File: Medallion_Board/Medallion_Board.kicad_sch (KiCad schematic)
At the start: 125 parts, among them IC1 Wio-SX1262, J1 SWD HEADER, J2 EXPANSION, J3 IPEX, J4 FH12-24S-0.5SH_55_, P1 JST_BTN_1, P2 JST_BTN_2, P3 JST_BTN_3, Q1 DMG3415U, Q2 Si1308EDL, U1 MDBT50Q-1MV2, U2 MAX17048G_T10, U3 LC86LICMD, U4 RT9080-33GJ5, U5 MCP73831T-2ACI_OT, U6 BNO085, U7 DRV2605LDGSR, U8 MX25R6435FZAIH0, X1 USB4085-GF-A, Y1 32.768KHZ

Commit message: Move to hierarchical schematic
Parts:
- removed BATT1: JST_PH, S2B-PH-SM4-TB_LF__SN_:JST_S2B-PH-SM4-TB_LF__SN_, symbol S2B-PH-SM4-TB_LF__SN_:S2B-PH-SM4-TB_LF__SN_
- removed C10, C15, C16, C17, C18, C19, C20, C21, C22, C23, C31, C32, C33, C34, C35, C36, C37, C38, C41: 0.1uF, Capacitor_SMD:C_0402_1005Metric, symbol Adafruit ESP32-S3 8MB No PSRAM-eagle-import:CAP_CERAMIC0805-NOOUTLINE
- removed C11, C12, C13, C14, C5, C9: 10uF, Capacitor_SMD:C_0805_2012Metric, symbol Adafruit ESP32-S3 8MB No PSRAM-eagle-import:CAP_CERAMIC0805-NOOUTLINE
- removed C24, C25, C27, C28, C7: 0.1uF, Capacitor_SMD:C_0402_1005Metric, symbol Adafruit ESP32-S3 8MB No PSRAM-eagle-import:CAP_CERAMIC0603_NO
- removed C26: 22uF, Capacitor_SMD:C_0402_1005Metric, symbol Adafruit ESP32-S3 8MB No PSRAM-eagle-import:CAP_CERAMIC0805-NOOUTLINE
- removed C29, C30: NM, Capacitor_SMD:C_0402_1005Metric, symbol Adafruit ESP32-S3 8MB No PSRAM-eagle-import:CAP_CERAMIC0805-NOOUTLINE
- removed C39, C40, C42, C45, C46, C47, C48, C49, C50, C51, C6: 1uF, Capacitor_SMD:C_0603_1608Metric, symbol Adafruit ESP32-S3 8MB No PSRAM-eagle-import:CAP_CERAMIC0603_NO
- removed C43, C44: 4.7uF, Capacitor_SMD:C_0603_1608Metric, symbol Adafruit ESP32-S3 8MB No PSRAM-eagle-import:CAP_CERAMIC0603_NO
- removed C8: 100mF, KW-5R5C104-R:CAPPRD500W60D1000H3150, symbol XH414HG-IV01E:XH414HG-IV01E
- removed CHG1: ORANGE, LED_SMD:LED_0603_1608Metric, symbol Adafruit ESP32-S3 8MB No PSRAM-eagle-import:LED0603_NOOUTLINE
- removed D1: MBR0540, Diode_SMD:D_SOD-123, symbol Adafruit ESP32-S3 8MB No PSRAM-eagle-import:DIODE-SCHOTTKYSOD-123
- removed D10, D11, D13, D14, D15, D16, D17, D18, D19, D20, D3, D4, D5, D6, D7, D8, D9: WS2812B2020, WS2812B2020:LED_WS2812B2020, symbol WS2812B2020:WS2812B2020
- removed D12: TPD1E05U06DPYR, TPD1E05U06DPYR:DIO_TPD1E05U06DPYR, symbol TPD1E05U06DPYR:TPD1E05U06DPYR
- removed D2: BAV199, BAV199:SOT23, symbol BAV199:BAV199
- removed D21, D22, D23: MBR0530, Diode_SMD:D_SOD-123, symbol Diode:MBR0530
- removed IC1: Wio-SX1262, 114993390:114993390, symbol 114993390:114993390
- removed J3: IPEX, RECE.20369:RECE20369001E01, symbol RECE_20369_001E_01:RECE.20369.001E.01
- removed J4: FH12-24S-0.5SH_55_, FH12-24S-0.5SH_55_:HRS_FH12-24S-0.5SH_55_, symbol FH12-24S-0.5SH_55_:FH12-24S-0.5SH_55_
- removed L1: 10uH, LQM18DN100M70L:INDC1608X95N, symbol LQM18DN100M70L:LQM18DN100M70L
- removed L2: 47uH 500mA, symbol LQM18DN100M70L:LQM18DN100M70L
- removed LRA1: Conn_01x02, Connector_PinHeader_2.54mm:PinHeader_1x02_P2.54mm_Vertical, symbol Connector_Generic:Conn_01x02
- removed ONOFF1: JST_ONOFF, SM02B-GHS-TB:JST_SM02B-GHS-TB, symbol SM02B-GHS-TB:SM02B-GHS-TB
- removed P1: JST_BTN_1, SM02B-GHS-TB:JST_SM02B-GHS-TB, symbol SM02B-GHS-TB:SM02B-GHS-TB
- removed P2: JST_BTN_2, SM02B-GHS-TB:JST_SM02B-GHS-TB, symbol SM02B-GHS-TB:SM02B-GHS-TB
- removed P3: JST_BTN_3, SM02B-GHS-TB:JST_SM02B-GHS-TB, symbol SM02B-GHS-TB:SM02B-GHS-TB
- removed Q1: DMG3415U, DMG3415U-7:SOT95P240X105-3N, symbol Adafruit ESP32-S3 8MB No PSRAM-eagle-import:MOSFET-P
- removed Q2: Si1308EDL, Package_TO_SOT_SMD:SOT-323_SC-70, symbol Transistor_FET:Si1308EDL
- removed R10, R11: 1K, Resistor_SMD:R_0603_1608Metric, symbol Adafruit ESP32-S3 8MB No PSRAM-eagle-import:RESISTOR_0603_NOOUT
- removed R12, R13, R16, R20, R22: 10K, Resistor_SMD:R_0603_1608Metric, symbol Adafruit ESP32-S3 8MB No PSRAM-eagle-import:RESISTOR_0603_NOOUT
- removed R14: 0R, Resistor_SMD:R_0402_1005Metric, symbol Adafruit ESP32-S3 8MB No PSRAM-eagle-import:RESISTOR_0603_NOOUT
- removed R15: 500R, Resistor_SMD:R_0603_1608Metric, symbol Adafruit ESP32-S3 8MB No PSRAM-eagle-import:RESISTOR_0603_NOOUT
- removed R17, R18: 5K, Resistor_SMD:R_0603_1608Metric, symbol Adafruit ESP32-S3 8MB No PSRAM-eagle-import:RESISTOR_0603_NOOUT
- removed R19, R21: 27R, Resistor_SMD:R_0603_1608Metric, symbol Adafruit ESP32-S3 8MB No PSRAM-eagle-import:RESISTOR_0603_NOOUT
- removed R23: 1M, Resistor_SMD:R_0603_1608Metric, symbol Adafruit ESP32-S3 8MB No PSRAM-eagle-import:RESISTOR_0603_NOOUT
- removed R24: 2.2R, Resistor_SMD:R_0603_1608Metric, symbol Adafruit ESP32-S3 8MB No PSRAM-eagle-import:RESISTOR_0603_NOOUT
- removed R9: 100K, Resistor_SMD:R_0603_1608Metric, symbol Adafruit ESP32-S3 8MB No PSRAM-eagle-import:RESISTOR_0603_NOOUT
- removed U1: MDBT50Q-1MV2, MDBT50Q-1MV2:XCVR_MDBT50Q-1MV2, symbol MDBT50Q-1MV2:MDBT50Q-1MV2
- removed U2: MAX17048G_T10, MAX17048G_T10:SON50P200X200X80-9N, symbol MAX17048G_T10:MAX17048G_T10
- removed U3: LC86LICMD, LC86LICMD:MODULE_LC86LICMD, symbol LC86LICMD:LC86LICMD
- removed U4: RT9080-33GJ5, RT9080-33GJ5:SOT94P280X100-5N, symbol Adafruit ESP32-S3 8MB No PSRAM-eagle-import:VREG_SOT23-5
- removed U5: MCP73831T-2ACI_OT, MCP73831T-2ACI_OT:SOT95P280X145-5N, symbol MCP73831T-2ACI_OT:MCP73831T-2ACI_OT
- removed U6: BNO085, BNO085:IC_BNO085, symbol BNO085:BNO085
- removed U7: DRV2605LDGSR, DRV2605LDGSR:SOP50P490X110-10N, symbol DRV2605LDGSR:DRV2605LDGSR
- removed U8: MX25R6435FZAIH0, MX25R6435FZAIH0:SON80P400X400X60-9N, symbol MX25R6435FZAIH0:MX25R6435FZAIH0
- added C5: 1uF, Capacitor_SMD:C_0603_1608Metric, symbol Adafruit ESP32-S3 8MB No PSRAM-eagle-import:CAP_CERAMIC0603_NO
- added C6: 0.1uF, Capacitor_SMD:C_0402_1005Metric, symbol Adafruit ESP32-S3 8MB No PSRAM-eagle-import:CAP_CERAMIC0805-NOOUTLINE
- added U1: BMD-340-A-R, BMD_340_A_R:RIGADO_BMD-340-A-R, symbol BMD-340-A-R:BMD-340-A-R
- added U2: MX25R6435FZAIH0, MX25R6435FZAIH0:SON80P400X400X60-9N, symbol MX25R6435FZAIH0:MX25R6435FZAIH0
- C1, C2: value 12pF -> 10uF; footprint Capacitor_SMD:C_0402_1005Metric -> Capacitor_SMD:C_0805_2012Metric; MPN GMC04CG120J6R3NT -> CL21A106KPFNNNG
- C3, C4: value 10uF -> 12pF; footprint Capacitor_SMD:C_0805_2012Metric -> Capacitor_SMD:C_0402_1005Metric; MPN 0805W106K6R3CC -> C0402C0G120J500NTB; PRICE 0.07 -> 0.00371
- R2: value 10K -> 5K; MPN RC0603FR-0710KL -> RT0603BRE075KL
- R3: value 10K -> 27R; MPN RC0603FR-0710KL -> RC0603FR-0727RL
- R4: value 100K -> 27R; MPN RC0603FR-07100KL -> RC0603FR-0727RL
- R5: value 1K -> 5K; MPN RC0603FR-071KL -> RT0603BRE075KL
- R6, R7: value 5K -> 10K; MPN RT0603BRE075KL -> RC0603FR-0710KL
- R8: value 2K -> 10K; MPN RC0603FR-072KL -> RC0603FR-0710KL
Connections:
- net GPIO15 is gone; now on net GPIO17: J2.2 (Pin_2)
- net VHI is gone; now on net D-: R4.1
- net D+: now also R3.1, U1.68 (USB-D+)
- net D-: now also U1.67 (USB-D-)
- net FLASH_CS: now also R8.1, U2.1 (CS#)
- net FLASH_RST: now also U2.7 (RESET#/SIO3)
- net FLASH_WP: now also U2.3 (WP#/SIO2)
- net GND: now also C1.2, C2.2, C3.1, C4.1, R1.1, R2.1, C5.2, C6.2, U1.1 (GND), U1.16 (GND__5), U1.18 (GND__6), U1.2 (GND__1), U1.29 (GND__7), U1.3 (GND__2), U1.30 (GND__8), U1.4 (GND__3), U1.45 (GND__9), U1.46 (GND__10), U1.47 (GND__11), U1.5 (GND__4), U1.55 (GND__12), U2.4 (GND); no longer C1.1, C2.1, C3.2, C4.2, R7.2, R8.1
- net GPIO17: now also U1.35 (P0.17); no longer J2.4 (Pin_4)
- net GPS_ANT_ACTIVE: now also U1.11 (P0.30)
- net GPS_RESET: now also U1.12 (P0.31)
- net GPS_WAKEUP: now also U1.10 (P0.29)
- net NEOPIX: now also U1.34 (P0.16)
- net OSC1: now also C3.2, U1.13 (P0.00); no longer C1.2
- net OSC2: now also C4.2, U1.14 (P0.01); no longer C2.2
- net RXD_GPS: now also U1.23 (P0.07)
- net SCL: now also R6.2, U1.8 (P0.27); no longer R2.1
- net SDA: now also R7.2, U1.7 (P0.26); no longer R3.1
- net SPI_MISO: now also U1.40 (P0.22), U2.2 (SO/SIO1)
- net SPI_MOSI: now also U1.41 (P0.23), U2.5 (SI/SIO0)
- net SPI_SCK: now also U1.42 (P0.24), U2.6 (SCLK)
- net TXD_GPS: now also U1.22 (P0.06)
- net VBUS: now also C2.1, U1.66 (VBUS)
- net uC_RESET: now also R5.1, C5.1, U1.39 (P0.18); no longer R1.1
- net at J1.3 (Pin_3): now also U1.44 (SWDIO)
- net at J1.2 (Pin_2): now also U1.43 (SWCLK)
- net +3.3V: now reaches R8.2
- net +3.3V: now also C1.1, J1.1 (Pin_1), J2.7 (Pin_7), R5.2, R6.1, R7.1, C6.1, U1.17 (VCC1), U1.65 (VCCH1), U2.8 (VCC)
- net at R4.2: now also X1.B6 (DP2)
- net at X1.B5 (CC2): now also R2.2
- net at X1.A6 (DP1): now also R3.2
- net at X1.A5 (CC1): now also R1.2
- removed net 3.3V: C4.1, J1.1 (VCC), J2.7 (Pin_7), R1.2, R2.2, R3.2
- net GPIO14 renamed GPIO05
- net GPIO05: now also U1.21 (P0.05)
- net GPIO16 renamed GPIO19
- net GPIO19: now also U1.37 (P0.19)
- new net Communications/LORA_BUSY: U1.33 (P0.15)
- new net Communications/LORA_DIO1: U1.25 (P0.09)
- new net Communications/LORA_NRST: U1.26 (P0.10)
- new net Communications/LORA_NSS: U1.31 (P0.13)
- new net Communications/LORA_RF_SW: U1.32 (P0.14)
- new net Communications/SPI_MISO: U1.28 (P0.12)
- new net Communications/SPI_MOSI: U1.27 (P0.11)
- new net Communications/SPI_SCK: U1.24 (P0.08)
- new net GPIO20: J2.4 (Pin_4), U1.38 (P0.20)
- new net HAPTIC_EN: U1.15 (P0.02)
- new net Power and USB/LOW_BATT: U1.36 (P0.21)
- new net User IO/BNO_NINT: U1.48 (P1.05)
- new net User IO/BNO_NRST: U1.49 (P1.06)
- new net User IO/DISP_BS: U1.56 (P1.00)
- new net User IO/DISP_BUSY: U1.57 (P1.01)
- new net User IO/DISP_CS: U1.58 (P1.02)
- new net User IO/DISP_D/C: U1.59 (P1.03)
- new net User IO/DISP_RES: U1.60 (P1.04)
- new net User IO/USER_BTN_1: U1.50 (P1.07)
- new net User IO/USER_BTN_2: U1.51 (P1.08)
- new net User IO/USER_BTN_3: U1.52 (P1.09)
- no-connect marks 14 -> 15
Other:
- added sheet Communications (communications.kicad_sch)
- added sheet Power and USB (power.kicad_sch)
- added sheet User IO (user_io.kicad_sch)
- note added: "FUTURE EXPANSION BREAKOUT"
- note added: "LOW FREQUENCY PINS (<10kHz) P0.28-0.31, P0.02, P0.03, P0.09, P0.10 P1.01-1.07, P1.10-1.15"
- note added: "RESET"
- note removed: "1.0K = 1000mA"
- note removed: "10K = 100mA"
- note removed: "2.0K = 500mA"
- note removed: "5.0K = 200mA"
- note removed: "Adafruit estimate 20mA for typical use 20mA * 4 = 80mA LED load"
- note removed: "CHARGER"
- note removed: "E-INK DISPLAY"
- note removed: "FUEL GAUGE"
- note removed: "FUTURE-PROOFING BREAKOUT"
- note removed: "GNSS"
- note removed: "HAPTICS"
- note removed: "IMU SENSOR"
- note removed: "LIPO CHARGING AND REPORTING"
- note removed: "LORA RADIO"
- note removed: "NEEDS REVIEW https://files.waveshare.com/wiki/1.54inch%20e-Paper%20Module%20(G)/1.54inch_e-Paper_(G).pdf PAGE 44"
- note removed: "Neopixel Ring"
- note removed: "No more than 3 pixels will be driven at full brightness, or 8 at 1/2 brightness, at a time."
- note removed: "POWER AND FILTERING"
- note removed: "USER BUTTONS"
- note removed: "Unused but implemented just in case"
- note removed: "V_BCKP enables much faster location acquisition 30s -> 2s"
- note removed: "nRF52840 MODULE"
- moved on the sheet: J2

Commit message: Some minor cleaning
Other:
- note added: "The product here is a smart compass. It has GNSS and an IMU for positioning in the world, and LoRa and BLE for comms. It uses a ring of RGB LED, an e-ink display, and haptic feedback for user interaction, along with 3 buttons. Battery powered, with USB-C charging."
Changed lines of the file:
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@@
 		(title "Smart Compass")
 		(date "2026-06-04")
+		(rev "0.2")
 	)
 	(rectangle
@@
 		)
 	)
+	(text "The product here is a smart compass. \n\nIt has GNSS and an IMU for positioning in the world,\nand LoRa and BLE for comms. \n\nIt uses a ring of RGB LED, an e-ink display, and haptic \nfeedback for user interaction, along with 3 buttons. \n\nBattery powered, with USB-C charging."
+		(exclude_from_sim no)
+		(at 239.014 30.226 0)
+		(effects
+			(font
+				(size 1.27 1.27)
+			)
+		)
+	)
 	(text "LOW FREQUENCY PINS\n(<10kHz)\n\nP0.28-0.31, P0.02, P0.03, P0.09, P0.10\nP1.01-1.07, P1.10-1.15"
 		(exclude_from_sim no)
@@
 		(property "Value" "GND"
 			(at 138.43 34.29 0)
+			(hide yes)
 			(show_name no)
 			(do_not_autoplace no)
@@
 		(property "Value" "GND"
 			(at 172.72 154.94 0)
+			(hide yes)
 			(show_name no)
 			(do_not_autoplace no)
@@
 		(property "Value" "GND"
 			(at 274.32 76.2 0)
+			(hide yes)
 			(show_name no)
 			(do_not_autoplace no)
@@
 		(property "Value" "GND"
 			(at 275.59 160.02 0)
+			(hide yes)
 			(show_name no)
 			(do_not_autoplace no)
@@
 		(property "Value" "GND"
 			(at 270.51 76.2 0)
+			(hide yes)
 			(show_name no)
 			(do_not_autoplace no)
@@
 		(property "Value" "GND"
 			(at 207.01 110.49 0)
+			(hide yes)
 			(show_name no)
 			(do_not_autoplace no)
@@
 		(property "Value" "GND"
 			(at 36.83 58.42 0)
+			(hide yes)
 			(show_name no)
 			(do_not_autoplace no)
@@
 		(property "Value" "GND"
 			(at 132.08 33.02 0)
+			(hide yes)
 			(show_name no)
 			(do_not_autoplace no)
@@
 		(property "Value" "GND"
 			(at 118.11 152.4 0)
+			(hide yes)
 			(show_name no)
 			(do_not_autoplace no)
@@
 		(property "Value" "GND"
 			(at 72.39 43.18 0)
+			(hide yes)
 			(show_name no)
 			(do_not_autoplace no)
@@
 		(property "Value" "GND"
 			(at 250.19 105.41 0)
+			(hide yes)
 			(show_name no)
 			(do_not_autoplace no)

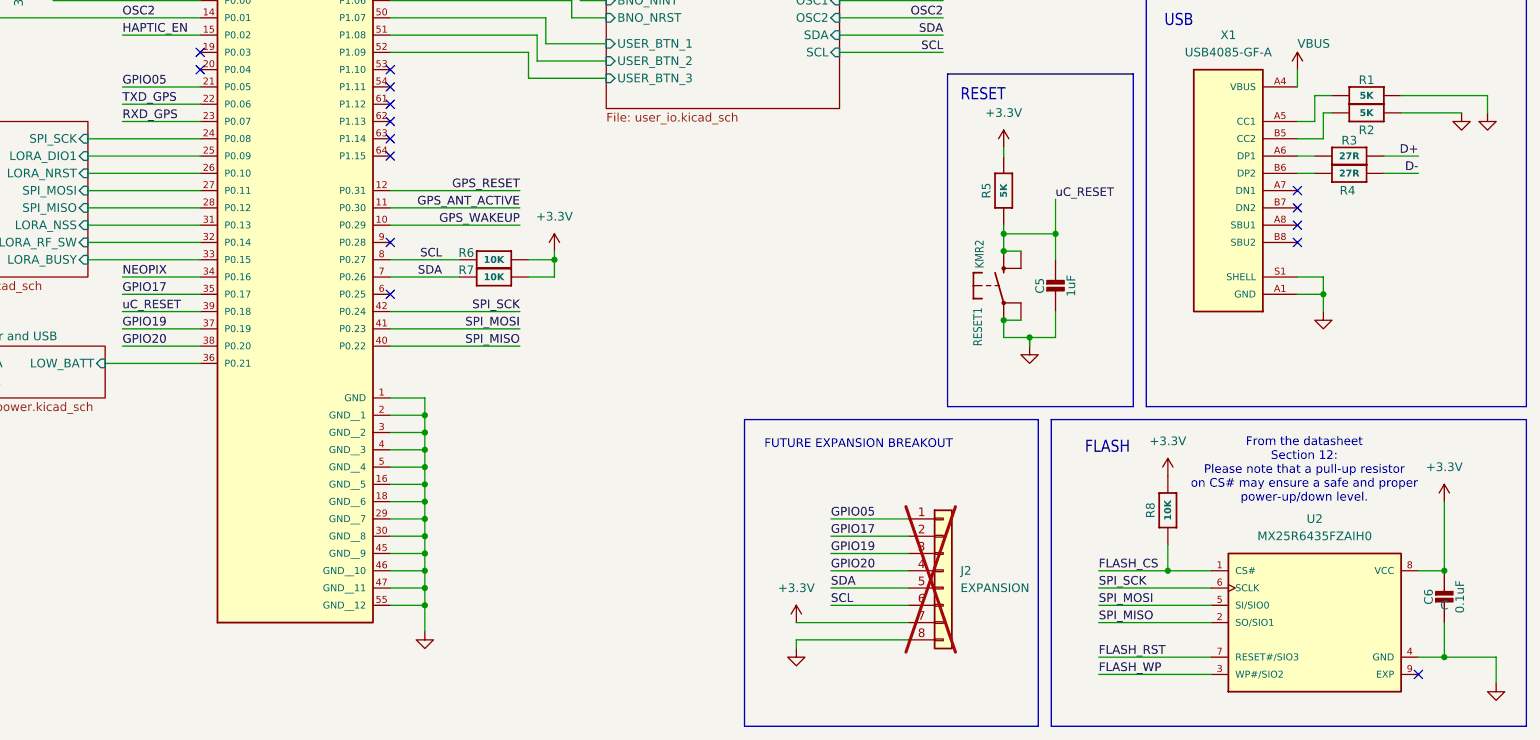
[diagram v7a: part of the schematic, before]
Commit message: Check over i2c, spi, and uart connections
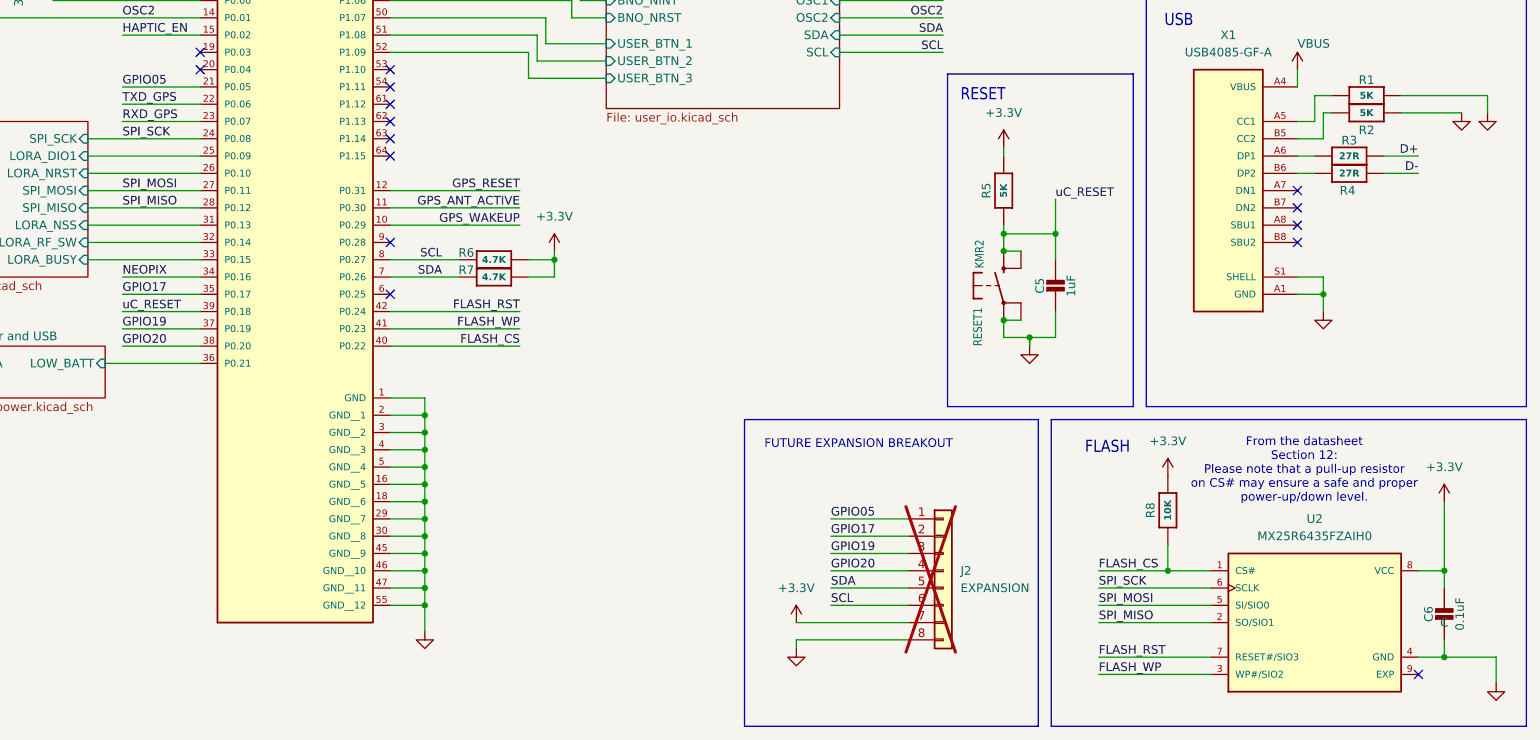
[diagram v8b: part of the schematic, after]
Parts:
- R6, R7: value 10K -> 4.7K; MPN RC0603FR-0710KL -> RC0603FR-074K7L
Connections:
- net Communications/SPI_MISO is gone; now on net SPI_MISO: U1.28 (P0.12)
- net Communications/SPI_MOSI is gone; now on net SPI_MOSI: U1.27 (P0.11)
- net Communications/SPI_SCK is gone; now on net SPI_SCK: U1.24 (P0.08)
- net FLASH_CS: now also U1.40 (P0.22)
- net FLASH_RST: now also U1.42 (P0.24)
- net FLASH_WP: now also U1.41 (P0.23)
- net SPI_MISO: no longer U1.40 (P0.22)
- net SPI_MOSI: no longer U1.41 (P0.23)
- net SPI_SCK: no longer U1.42 (P0.24)
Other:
- moved on the sheet: C6
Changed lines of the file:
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@@
 	)
 	(junction
-		(at 267.97 138.43)
-		(diameter 0)
-		(color 0 0 0 0)
-	)
-	(junction
 		(at 118.11 138.43)
 		(diameter 0)
@@
 	)
 	(junction
-		(at 267.97 151.13)
-		(diameter 0)
-		(color 0 0 0 0)
-	)
-	(junction
 		(at 118.11 135.89)
 		(diameter 0)
@@
 	)
 	(junction
+		(at 267.97 151.13)
+		(diameter 0)
+		(color 0 0 0 0)
+	)
+	(junction
 		(at 118.11 128.27)
 		(diameter 0)
@@
 	)
 	(junction
+		(at 267.97 138.43)
+		(diameter 0)
+		(color 0 0 0 0)
+	)
+	(junction
 		(at 207.01 104.14)
 		(diameter 0)
@@
 	(wire
 		(pts
-			(xy 267.97 146.05) (xy 267.97 151.13)
+			(xy 267.97 148.59) (xy 267.97 151.13)
 		)
 		(stroke
@@
 	(wire
 		(pts
+			(xy 113.03 100.33) (xy 132.08 100.33)
+		)
+		(stroke
+			(width 0)
+			(type default)
+		)
+	)
+	(wire
+		(pts
 			(xy 134.62 59.69) (xy 134.62 63.5)
 		)
@@
 	(wire
 		(pts
-			(xy 113.03 100.33) (xy 132.08 100.33)
-		)
-		(stroke
-			(width 0)
-			(type default)
-		)
-	)
-	(wire
-		(pts
 			(xy 250.19 97.79) (xy 246.38 97.79)
 		)
@@
 	(wire
 		(pts
+			(xy 113.03 102.87) (xy 132.08 102.87)
+		)
+		(stroke
+			(width 0)
+			(type default)
+		)
+	)
+	(wire
+		(pts
 			(xy 113.03 125.73) (xy 118.11 125.73)
 		)
@@
 	(wire
 		(pts
-			(xy 118.11 135.89) (xy 118.11 138.43)
+			(xy 113.03 105.41) (xy 132.08 105.41)
 		)
 		(stroke
@@
 	(wire
 		(pts
-			(xy 81.28 44.45) (xy 85.09 44.45)
+			(xy 118.11 135.89) (xy 118.11 138.43)
 		)
 		(stroke
@@
 	(wire
 		(pts
-			(xy 132.08 105.41) (xy 113.03 105.41)
+			(xy 81.28 44.45) (xy 85.09 44.45)
 		)
 		(stroke
@@
 	(wire
 		(pts
+			(xy 267.97 140.97) (xy 267.97 138.43)
+		)
+		(stroke
+			(width 0)
+			(type default)
+		)
+	)
+	(wire
+		(pts
 			(xy 43.18 44.45) (xy 41.91 44.45)
 		)
@@
 	(wire
 		(pts
-			(xy 113.03 102.87) (xy 132.08 102.87)
-		)
-		(stroke
-			(width 0)
-			(type default)
-		)
-	)
-	(wire
-		(pts
 			(xy 68.58 80.01) (xy 85.09 80.01)
 		)
@@
 		)
 	)
+	(label "FLASH_WP"
+		(at 132.08 102.87 180)
+		(effects
+			(font
+				(size 1.27 1.27)
+			)
+			(justify right bottom)
+		)
+	)
 	(label "GPIO05"
 		(at 177.8 130.81 0)
@@
 		)
 	)
-	(label "SPI_SCK"
-		(at 132.08 100.33 180)
-		(effects
-			(font
-				(size 1.27 1.27)
-			)
-			(justify right bottom)
-		)
-	)
 	(label "OSC1"
 		(at 194.31 54.61 180)
@@
 		)
 	)
-	(label "SPI_MOSI"
-		(at 132.08 102.87 180)
-		(effects
-			(font
-				(size 1.27 1.27)
-			)
-			(justify right bottom)
-		)
-	)
 	(label "HAPTIC_EN"
 		(at 194.31 44.45 180)
@@
 		)
 	)
+	(label "FLASH_CS"
+		(at 132.08 105.41 180)
+		(effects
+			(font
+				(size 1.27 1.27)
+			)
+			(justify right bottom)
+		)
+	)
 	(label "uC_RESET"
 		(at 78.74 35.56 180)
@@
 		)
 	)
+	(label "FLASH_RST"
+		(at 132.08 100.33 180)
+		(effects
+			(font
+				(size 1.27 1.27)
+			)
+			(justify right bottom)
+		)
+	)
 	(label "SCL"
 		(at 120.65 92.71 180)
@@
 		)
 	)
+	(label "SPI_SCK"
+		(at 73.66 74.93 0)
+		(effects
+			(font
+				(size 1.27 1.27)
+			)
+			(justify left bottom)
+		)
+	)
 	(label "FLASH_WP"
 		(at 217.17 153.67 0)
@@
 		)
 	)
-	(label "SDA"
-		(at 177.8 140.97 0)
+	(label "SPI_MOSI"
+		(at 73.66 82.55 0)
 		(effects
 			(font
@@
 		)
 	)
-	(label "SPI_SCK"
-		(at 194.31 46.99 180)
+	(label "SDA"
+		(at 177.8 140.97 0)
 		(effects
 			(font
 				(size 1.27 1.27)
 			)
-			(justify right bottom)
+			(justify left bottom)
 		)
 	)
-	(label "SPI_MISO"
-		(at 132.08 105.41 180)
+	(label "SPI_SCK"
+		(at 194.31 46.99 180)
 		(effects
 			(font
@@
 		)
 	)
+	(label "SPI_MISO"
+		(at 73.66 85.09 0)
+		(effects
+			(font
+				(size 1.27 1.27)
+			)
+			(justify left bottom)
+		)
+	)
 	(label "SCL"
 		(at 177.8 143.51 0)
@@
 			)
 		)
-		(property "Value" "10K"
+		(property "Value" "4.7K"
 			(at 128.27 92.71 0)
 			(show_name no)
@@
 			)
 		)
-		(property "MPN" "RC0603FR-0710KL"
+		(property "MPN" "RC0603FR-074K7L"
 			(at 128.27 92.71 0)
 			(hide yes)
@@
 	(symbol
 		(lib_id "Adafruit ESP32-S3 8MB No PSRAM-eagle-import:CAP_CERAMIC0805-NOOUTLINE")
-		(at 267.97 143.51 0)
+		(at 267.97 146.05 0)
 		(unit 1)
 		(body_style 1)
@@
 		(dnp no)
 		(property "Reference" "C6"
-			(at 265.68 142.26 90)
+			(at 265.68 144.8 90)
 			(show_name no)
 			(do_not_autoplace no)
@@
 		)
 		(property "Value" "0.1uF"
-			(at 270.27 142.26 90)
+			(at 270.27 144.8 90)
 			(show_name no)
 			(do_not_autoplace no)
@@
 		)
 		(property "Footprint" "Capacitor_SMD:C_0402_1005Metric"
-			(at 267.97 143.51 0)
+			(at 267.97 146.05 0)
 			(hide yes)
 			(show_name no)
@@
 		)
 		(property "Datasheet" ""
-			(at 267.97 143.51 0)
+			(at 267.97 146.05 0)
 			(hide yes)
 			(show_name no)
@@
 		)
 		(property "Description" ""
-			(at 267.97 143.51 0)
+			(at 267.97 146.05 0)
 			(hide yes)
 			(show_name no)
@@
 		)
 		(property "REV" "C"
-			(at 267.97 143.51 0)
+			(at 267.97 146.05 0)
 			(show_name no)
 			(do_not_autoplace no)
@@
 		)
 		(property "MPN" "0402B104K160HI"
-			(at 267.97 143.51 90)
+			(at 267.97 146.05 90)
 			(hide yes)
 			(show_name no)
@@
 		)
 		(property "PRICE" "0.02134"
-			(at 267.97 143.51 90)
+			(at 267.97 146.05 90)
 			(hide yes)
 			(show_name no)
@@
 		)
 		(property "MAXIMUM_PACKAGE_HIEGHT" ""
-			(at 267.97 143.51 90)
+			(at 267.97 146.05 90)
 			(hide yes)
 			(show_name no)
@@
 			)
 		)
-		(property "Value" "10K"
+		(property "Value" "4.7K"
 			(at 128.27 95.25 0)
 			(show_name no)
@@
 			)
 		)
-		(property "MPN" "RC0603FR-0710KL"
+		(property "MPN" "RC0603FR-074K7L"
 			(at 128.27 95.25 0)
 			(hide yes)
